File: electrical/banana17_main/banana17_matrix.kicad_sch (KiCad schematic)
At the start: 36 parts, among them SW1 SW, SW10 SW, SW11 SW, SW12 SW, SW13 SW, SW14 SW, SW15 SW, SW16 SW, SW17 SW, SW18 SW, SW2 SW, SW3 SW, SW4 SW, SW5 RotaryEncoder_Switch, SW6 SW, SW7 SW, SW8 SW, SW9 SW

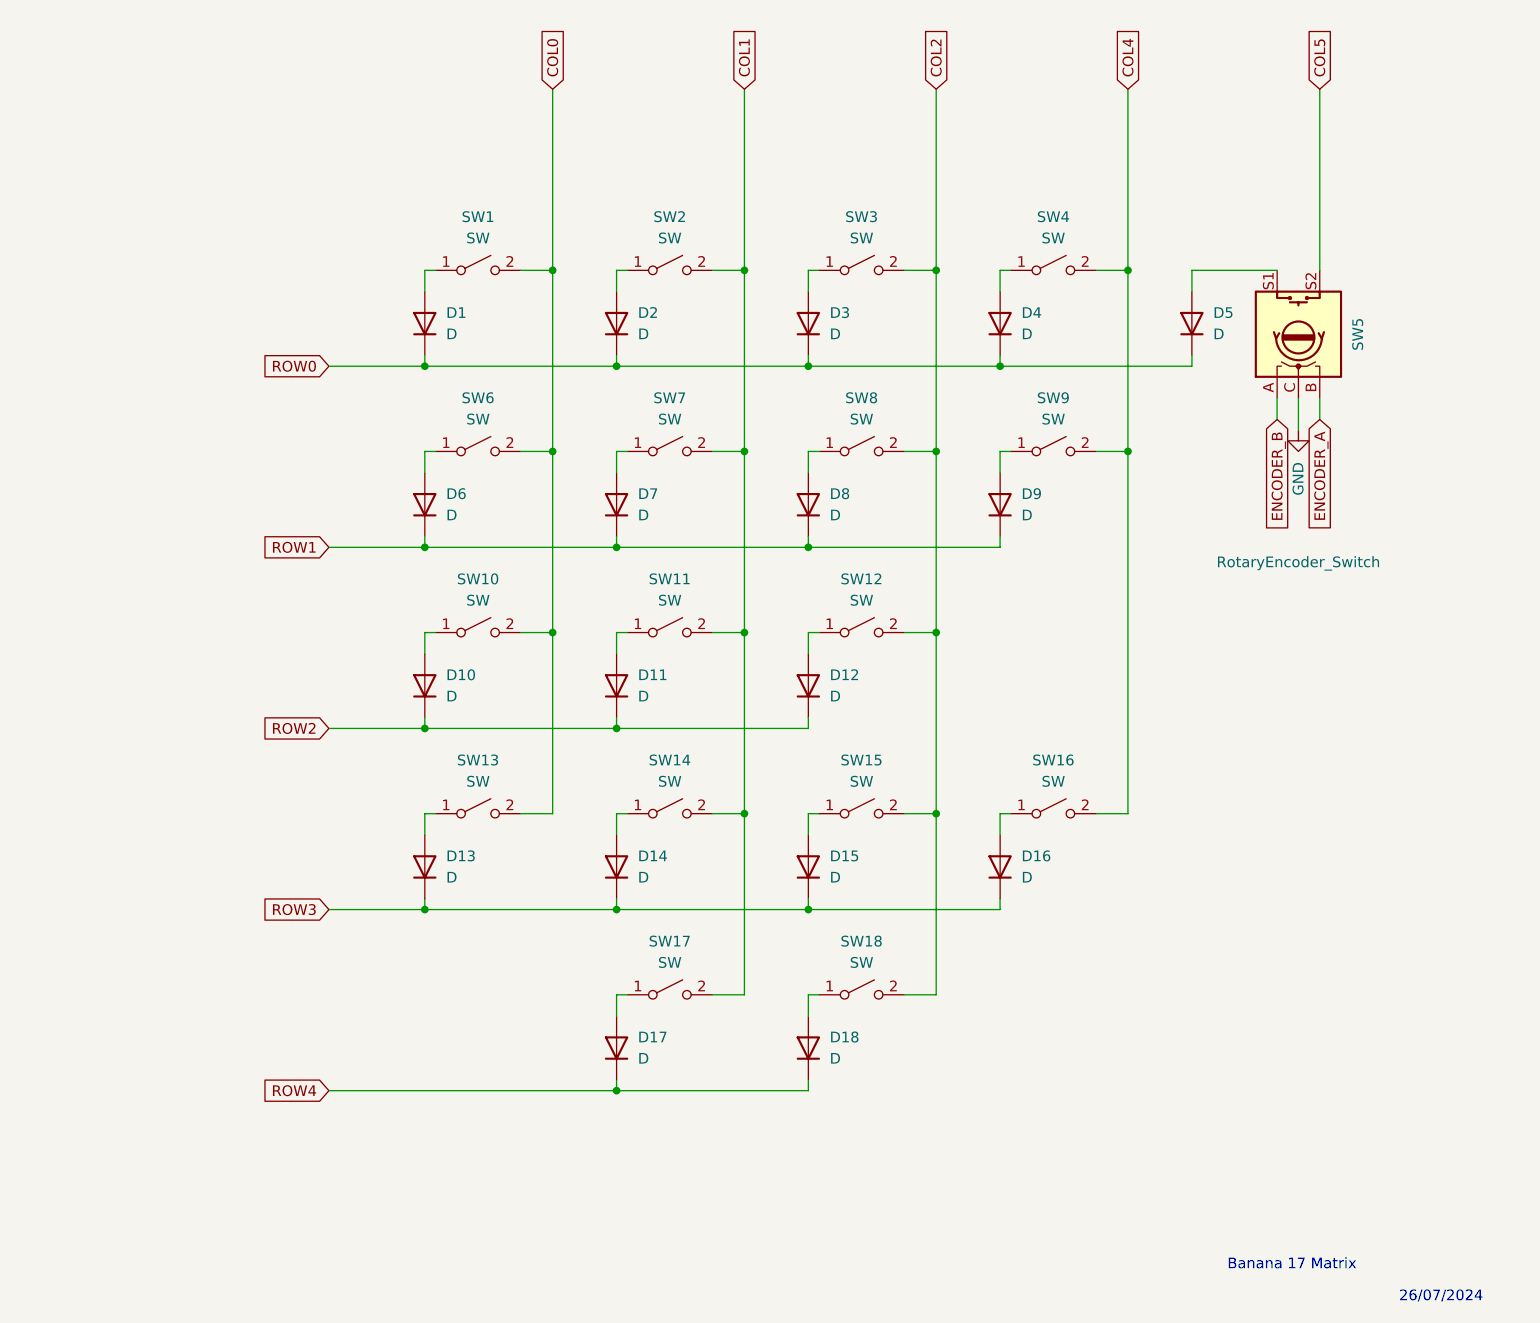
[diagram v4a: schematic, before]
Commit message: MX footprint updated with hotswappable socket.
MX footprint updated with hotswappable socket. Some issues with KiCAD plugin for keyboard layout editor, switches not aligning.
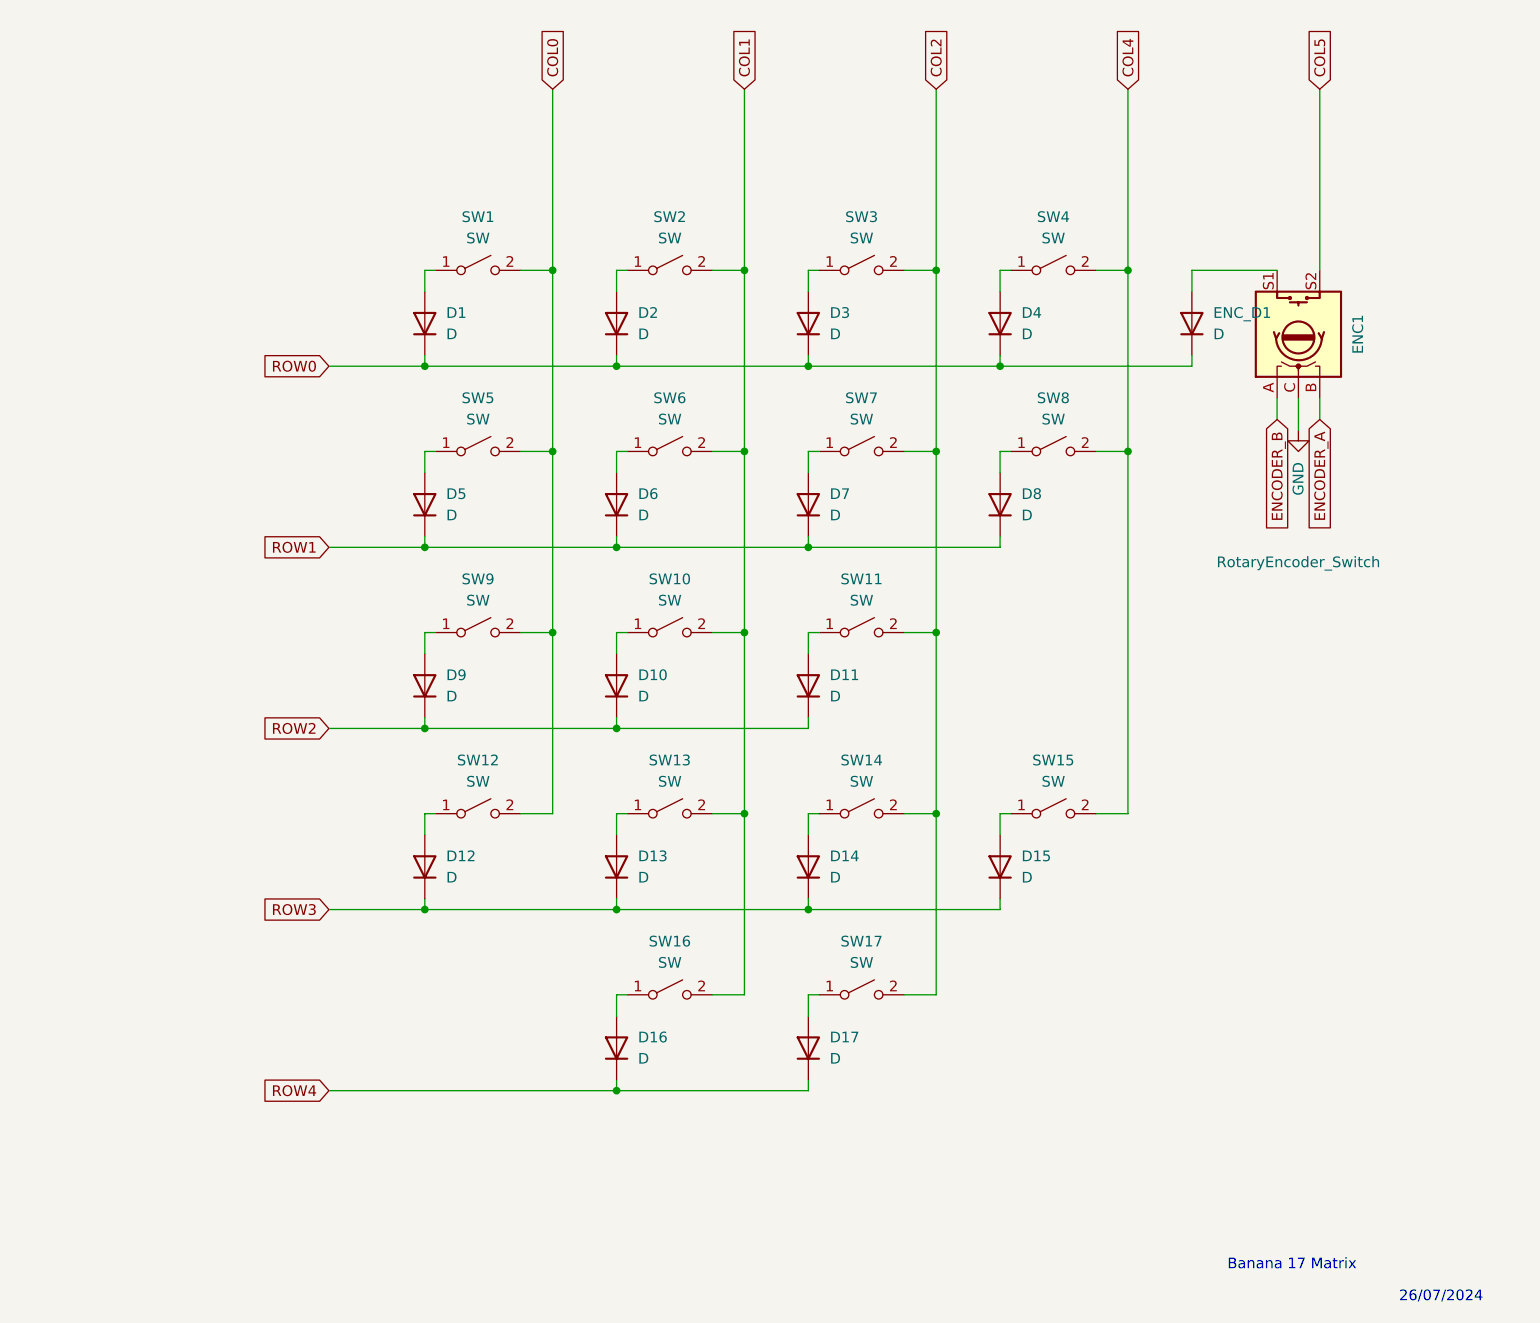
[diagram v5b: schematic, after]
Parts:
- SW1, SW2, SW3, SW4: footprint Button_Switch_Keyboard:SW_Cherry_MX_1.00u_PCB -> MX_Hotswap:MX-Hotswap-1U
- SW10: renamed from SW11; footprint Button_Switch_Keyboard:SW_Cherry_MX_1.00u_PCB -> MX_Hotswap:MX-Hotswap-1U
- SW11: renamed from SW12; footprint Button_Switch_Keyboard:SW_Cherry_MX_1.00u_PCB -> MX_Hotswap:MX-Hotswap-1U
- SW12: renamed from SW13; footprint Button_Switch_Keyboard:SW_Cherry_MX_1.00u_PCB -> MX_Hotswap:MX-Hotswap-1U
- SW13: renamed from SW14; footprint Button_Switch_Keyboard:SW_Cherry_MX_1.00u_PCB -> MX_Hotswap:MX-Hotswap-1U
- SW14: renamed from SW15; footprint Button_Switch_Keyboard:SW_Cherry_MX_1.00u_PCB -> MX_Hotswap:MX-Hotswap-1U
- SW15: renamed from SW16; footprint Button_Switch_Keyboard:SW_Cherry_MX_2.00u_Vertical_PCB -> MX_Hotswap:MX-Hotswap-1U
- SW16: renamed from SW17; footprint Button_Switch_Keyboard:SW_Cherry_MX_2.00u_PCB -> MX_Hotswap:MX-Hotswap-1U
- SW17: renamed from SW18; footprint Button_Switch_Keyboard:SW_Cherry_MX_1.00u_PCB -> MX_Hotswap:MX-Hotswap-1U
- SW5: renamed from SW6; footprint Button_Switch_Keyboard:SW_Cherry_MX_1.00u_PCB -> MX_Hotswap:MX-Hotswap-1U
- SW6: renamed from SW7; footprint Button_Switch_Keyboard:SW_Cherry_MX_1.00u_PCB -> MX_Hotswap:MX-Hotswap-1U
- SW7: renamed from SW8; footprint Button_Switch_Keyboard:SW_Cherry_MX_1.00u_PCB -> MX_Hotswap:MX-Hotswap-1U
- SW8: renamed from SW9; footprint Button_Switch_Keyboard:SW_Cherry_MX_2.00u_Vertical_PCB -> MX_Hotswap:MX-Hotswap-1U
- SW9: renamed from SW10; footprint Button_Switch_Keyboard:SW_Cherry_MX_1.00u_PCB -> MX_Hotswap:MX-Hotswap-1U
- renumbered D11 to D10, D12 to D11, D13 to D12, D14 to D13, D15 to D14, D16 to D15, D17 to D16, D18 to D17, D6 to D5, D7 to D6, D8 to D7, D9 to D8, D10 to D9, SW5 to ENC1, D5 to ENC_D1

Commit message: Switches positioned in matrix. Working on positioning the RP2040.
Switches positioned in matrix. Working on positioning the RP2040.
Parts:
- SW15, SW8: footprint MX_Hotswap:MX-Hotswap-1U -> MX_Hotswap:MX-Hotswap-2U-Vertical
- SW16: footprint MX_Hotswap:MX-Hotswap-1U -> MX_Hotswap:MX-Hotswap-2U
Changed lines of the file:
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@@
 			)
 		)
-		(property "Footprint" "MX_Hotswap:MX-Hotswap-1U"
+		(property "Footprint" "MX_Hotswap:MX-Hotswap-2U-Vertical"
 			(at 166.37 135.89 0)
 			(effects
@@
 			)
 		)
-		(property "Footprint" "MX_Hotswap:MX-Hotswap-1U"
+		(property "Footprint" "MX_Hotswap:MX-Hotswap-2U"
 			(at 120.65 157.48 0)
 			(effects
@@
 			)
 		)
-		(property "Footprint" "MX_Hotswap:MX-Hotswap-1U"
+		(property "Footprint" "MX_Hotswap:MX-Hotswap-2U-Vertical"
 			(at 166.37 92.71 0)
 			(effects

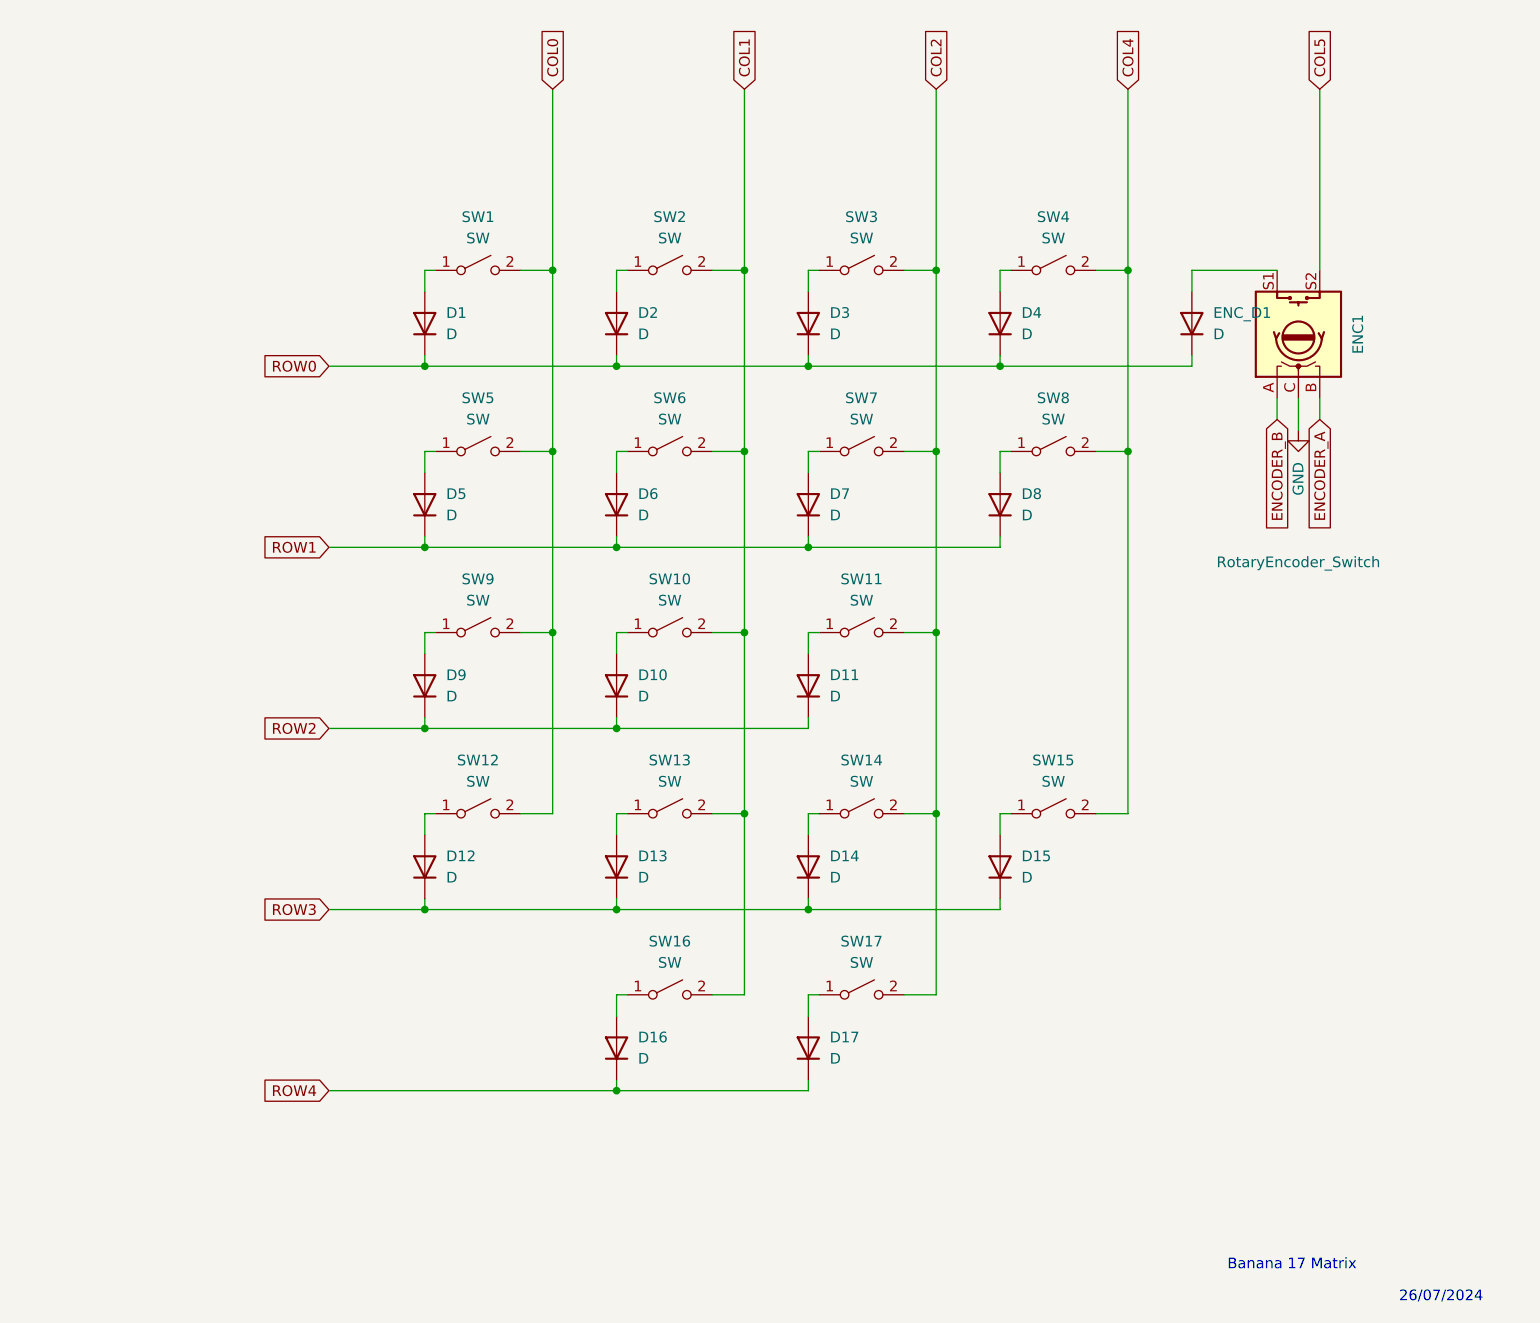
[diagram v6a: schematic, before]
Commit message: Added second rotary encoder.
Added second rotary encoder.
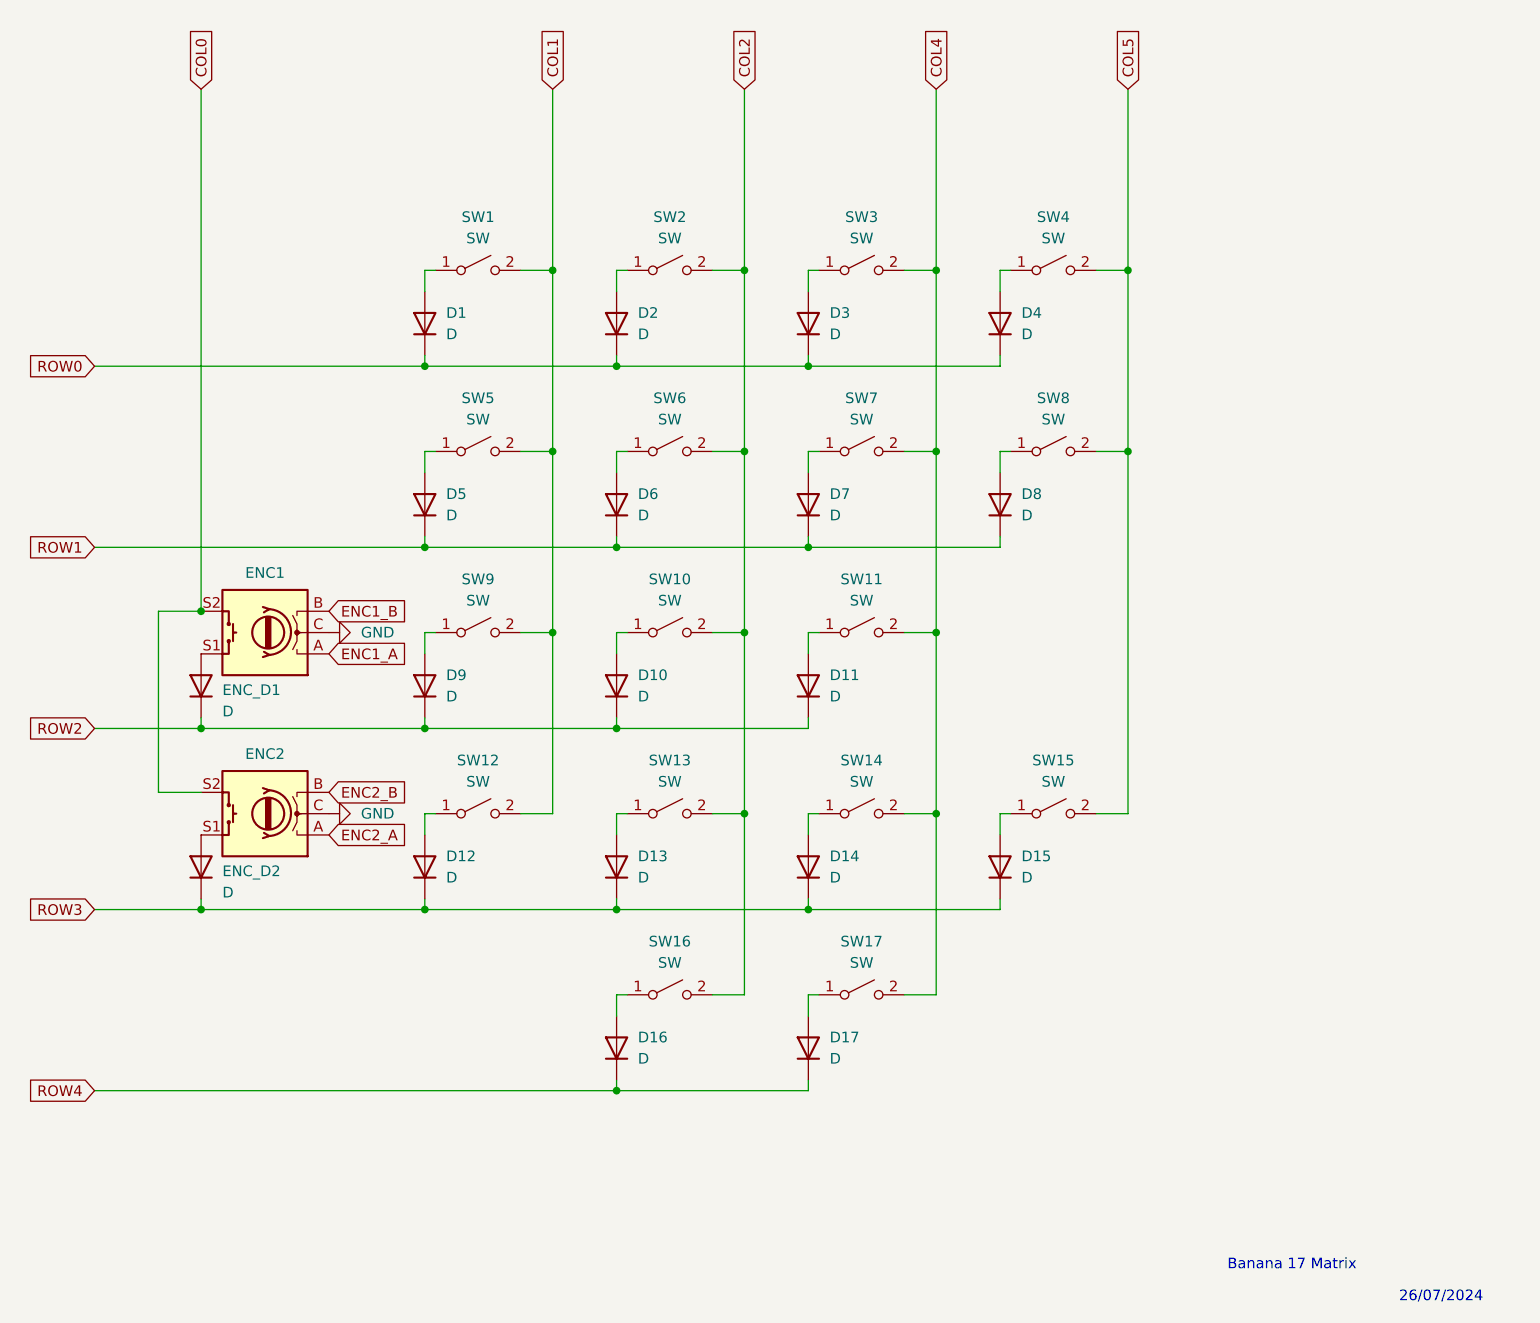
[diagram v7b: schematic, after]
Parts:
- added ENC2: RotaryEncoder_Switch, Rotary_Encoder:RotaryEncoder_Alps_EC11E-Switch_Vertical_H20mm, symbol Device:RotaryEncoder_Switch
- added ENC_D2: D, Diode_SMD:D_0805_2012Metric_Pad1.15x1.40mm_HandSolder, symbol Device:D
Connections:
- net COL0: now also ENC1.S2, ENC2.S2; no longer SW1.2 (B), SW12.2 (B), SW5.2 (B), SW9.2 (B)
- net COL1: now also SW1.2 (B), SW12.2 (B), SW5.2 (B), SW9.2 (B); no longer SW10.2 (B), SW13.2 (B), SW16.2 (B), SW2.2 (B), SW6.2 (B)
- net COL2: now also SW10.2 (B), SW13.2 (B), SW16.2 (B), SW2.2 (B), SW6.2 (B); no longer SW11.2 (B), SW14.2 (B), SW17.2 (B), SW3.2 (B), SW7.2 (B)
- net COL4: now also SW11.2 (B), SW14.2 (B), SW17.2 (B), SW3.2 (B), SW7.2 (B); no longer SW15.2 (B), SW4.2 (B), SW8.2 (B)
- net COL5: now also SW15.2 (B), SW4.2 (B), SW8.2 (B); no longer ENC1.S2
- net GND: now also ENC2.C
- net ROW0: no longer ENC_D1.1 (K)
- net ROW2: now also ENC_D1.1 (K)
- net ROW3: now also ENC_D2.1 (K)
- net ENCODER_A renamed ENC1_B
- net ENCODER_B renamed ENC1_A
- new net: ENC2.S1, ENC_D2.2 (A)
- new net ENC2_A: ENC2.A
- new net ENC2_B: ENC2.B
